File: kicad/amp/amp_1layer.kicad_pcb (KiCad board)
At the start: 2 copper layers, 194.3 x 100 mm, 134 parts, among them J1 DC 12V IN, J2 IN L-G-R, J3 SPK L, J4 SPK R, Q1001 BC547, Q1002 BC547, Q1003 BC557, Q1004 BD139, Q1005 BD140, Q1006 BC547, Q2001 BC547, Q2002 BC547, Q2003 BC557, Q2004 BD139, Q2005 BD140, Q2006 BC547

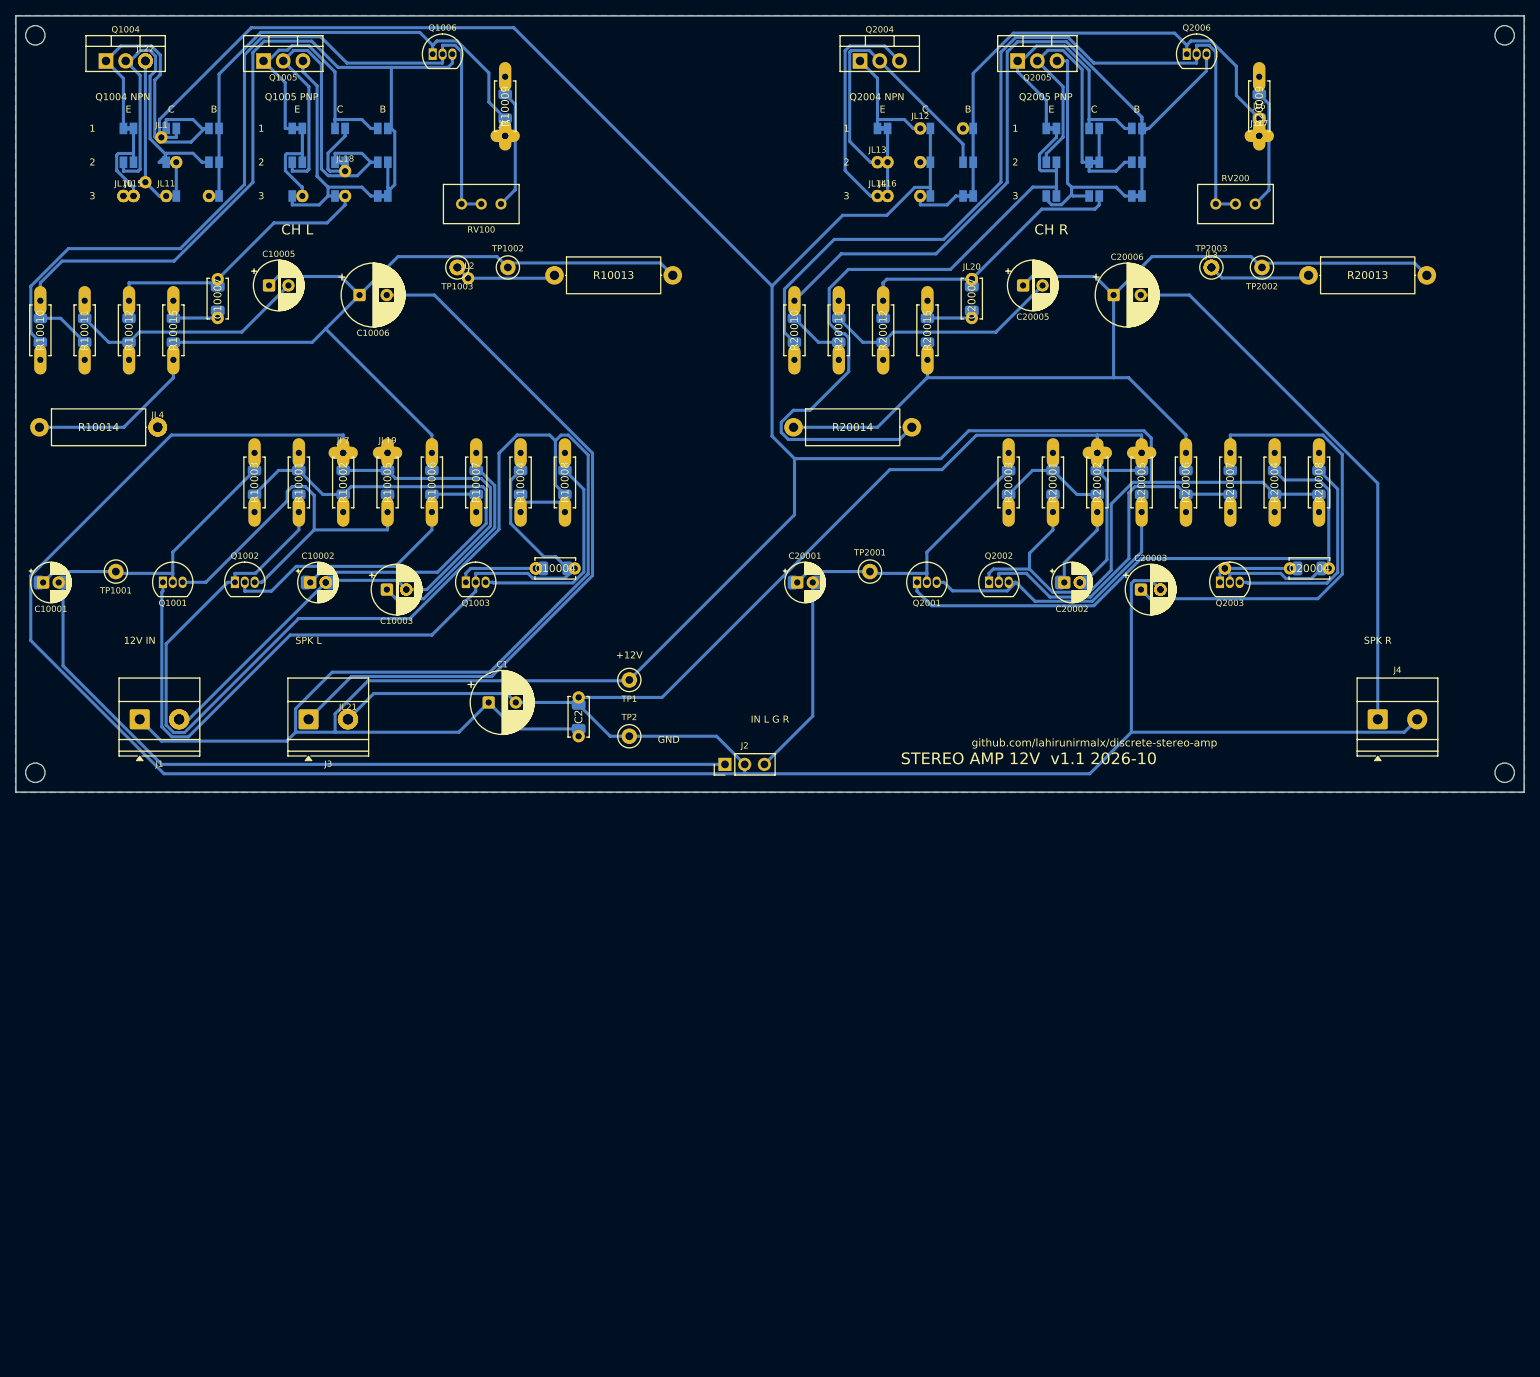
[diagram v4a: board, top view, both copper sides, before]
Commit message: Release 1.2: mirror-loaded front end, closed-loop PSU, VU tap, headphone board
- Amp: PNP input pair with NPN current-mirror load, LED-referenced current-source tail,
  NPN VAS with bootstrapped load from +12V, 220p Miller + 47p lead cap (THD 0.004% at 26 mW/8R,
  0.019% at 0.29 W; was 0.03 / 0.2). 1k VU meter tap per channel to header J5.
- PSU: BC547 error amplifier, 5.6 V zener fed from VOUT, 8.2k + 2k trimmer / 10k divider,
  2.2k drive, 47n/100n compensation. 12.0 V set point, 0.14 V dip on a 1 A step.
- New headphone board (DPDT switch, 120R series, DIRECT jumpers, 3.5 mm jack, panel-jack header).
- Boards: amp 134x85 / compact 100x98, PSU 90x58, hp 42x30; panel 155x155 with four boards.
  All 2-layer boards and the panel DRC clean; single-sided amp down to 15 errors.
- Toolchain: STAMP constant, reroute.sh second routing pass, rotated titles, link holes on
  jumper pads, 2 mm routing corridor per channel.
- Docs, BOMs, order guide, changelog, known issues rewritten for release 2.
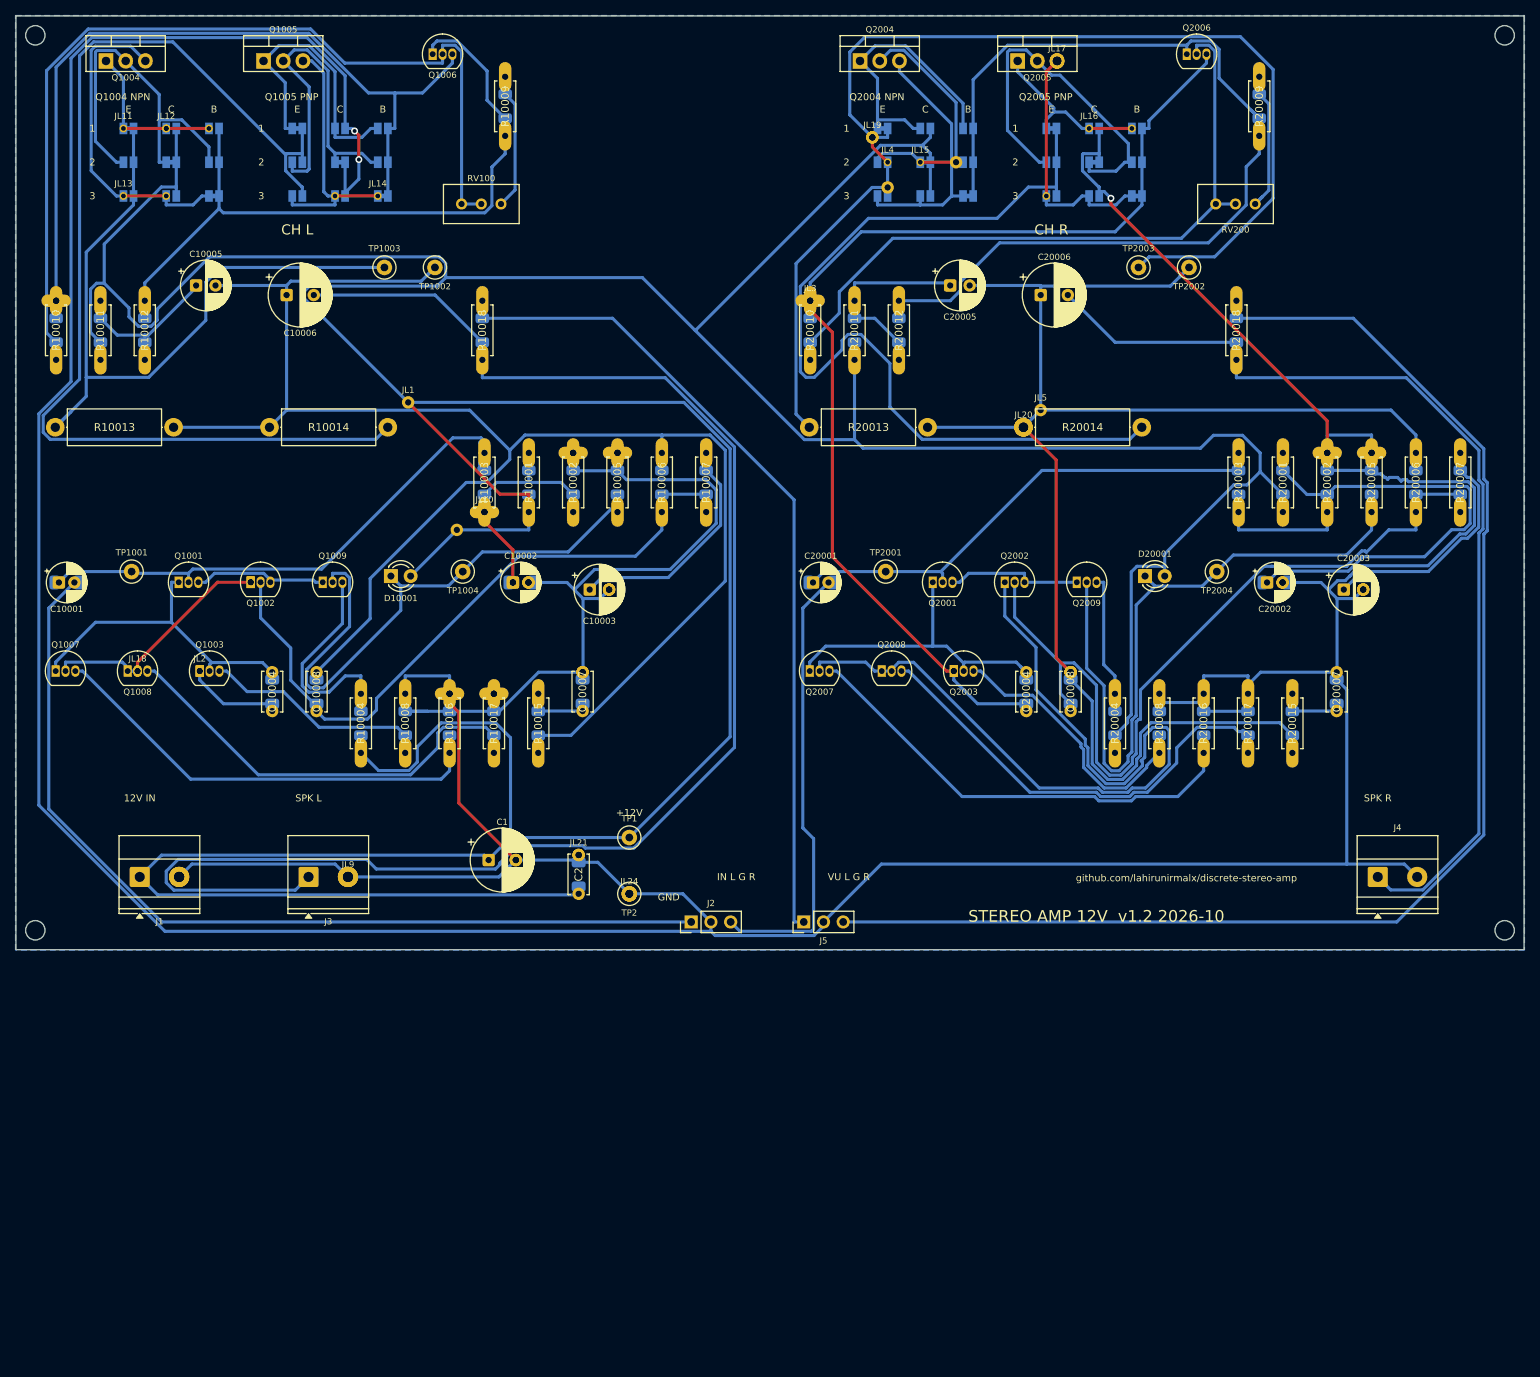
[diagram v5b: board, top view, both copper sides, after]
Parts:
- added C10008: 47p, Custom:C_P5_1206, F.Cu at (88.7, 139.6)
- added C20008: 47p, Custom:C_P5_1206, F.Cu at (185.9, 139.6)
- added D10001: LED red, LED_THT:LED_D3.0mm, F.Cu at (98.3, 122.2)
- added D20001: LED red, LED_THT:LED_D3.0mm, F.Cu at (195.5, 122.2)
- added J5: VU L-G-R, Connector_PinHeader_2.54mm:PinHeader_1x03_P2.54mm_Vertical, F.Cu at (151.5, 166.7)
- added JL23: wire link, Custom:WireLink, F.Cu at (116.0, 123.0)
- added JL24: wire link, Custom:WireLink, F.Cu at (129.0, 163.1)
- added Q1007: BC547, Custom:TO92_SOT23, F.Cu at (55.1, 134.4)
- added Q1008: BC547, Custom:TO92_SOT23, F.Cu at (64.4, 134.4)
- added Q1009: BC557, Custom:TO92_SOT23, F.Cu at (89.5, 123.0)
- added Q2007: BC547, Custom:TO92_SOT23, F.Cu at (152.3, 134.4)
- added Q2008: BC547, Custom:TO92_SOT23, F.Cu at (161.5, 134.4)
- added Q2009: BC557, Custom:TO92_SOT23, F.Cu at (186.7, 123.0)
- added R10016: 100, Custom:R_Axial_1206, F.Cu at (105.9, 144.9)
- added R10017: 100, Custom:R_Axial_1206, F.Cu at (111.6, 144.9)
- added R10018: 1k, Custom:R_Axial_1206, F.Cu at (110.1, 94.3)
- added R20016: 100, Custom:R_Axial_1206, F.Cu at (203.0, 144.9)
- added R20017: 100, Custom:R_Axial_1206, F.Cu at (208.7, 144.9)
- added R20018: 1k, Custom:R_Axial_1206, F.Cu at (207.2, 94.3)
- added TP1004: LED 10.2V, TestPoint:TestPoint_Loop_D2.50mm_Drill1.0mm, F.Cu at (107.6, 121.6)
- added TP2004: LED 10.2V, TestPoint:TestPoint_Loop_D2.50mm_Drill1.0mm, F.Cu at (204.7, 121.6)
- C10004, C20004: value 100p -> 220p
- Q1001, Q1002, Q2001, Q2002: value BC547 -> BC557
- Q1003, Q2003: value BC557 -> BC547
- R10004, R20004: value 4.7k -> 1.2k
- R10005, R20005: value 10k -> 4.7k
- TP1001, TP2001: value B1 5.9V -> B1 6.1V
- moved JL22 161.2 mm to (213.2, 123.0)
- moved JL6 135.3 mm to (114.4, 158.8)
- moved JL7 132.6 mm to (223.6, 123.9)
- moved JL9 111.0 mm to (92.8, 160.9)
- moved JL15 101.5 mm to (166.5, 68.8)
- moved JL4 100.0 mm to (162.3, 68.8)
- moved JL13 97.2 mm to (63.9, 73.2)
- moved JL12 97.1 mm to (69.4, 64.5)
- moved JL5 77.5 mm to (182.0, 100.8)
- moved JL19 74.5 mm to (160.3, 65.7)
- moved JL8 71.0 mm to (126.4, 123.9)
- moved JL18 69.7 mm to (65.7, 134.4)
- moved R10015 69.1 mm to (117.3, 144.9)
- moved R20015 69.1 mm to (214.4, 144.9)
- moved C10007 69.1 mm to (123.0, 139.6)
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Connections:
- C10004 pad 1: /VAS_L -> /B5_L
- C10004 pad 1S: /VAS_L -> /B5_L
- C10005 pad 1: /OUT_L -> Net-(C10005-Pad1)
- C10005 pad 2: Net-(C10005-Pad2) -> /OUT_L
- C20004 pad 1: /VAS_R -> /B5_R
- C20004 pad 1S: /VAS_R -> /B5_R
- C20005 pad 1: /OUT_R -> Net-(C20005-Pad1)
- C20005 pad 2: Net-(C20005-Pad2) -> /OUT_R
- JL10 pad 1: Net-(JP10007-A) -> Net-(C10002-Pad1)
- JL10 pad 2: Net-(JP10007-A) -> Net-(C10002-Pad1)
- JL11 pad 1: Net-(JP10007-A) -> Net-(JP10001-A)
- JL11 pad 2: Net-(JP10007-A) -> Net-(JP10001-A)
- JL12 pad 1: Net-(JP20001-A) -> Net-(JP10001-A)
- JL12 pad 2: Net-(JP20001-A) -> Net-(JP10001-A)
- JL13 pad 1: Net-(JP20004-A) -> Net-(JP10007-A)
- JL13 pad 2: Net-(JP20004-A) -> Net-(JP10007-A)
- JL14 pad 1: Net-(JP20007-A) -> Net-(JP10017-A)
- JL14 pad 2: Net-(JP20007-A) -> Net-(JP10017-A)
- JL15 pad 1: /E4_L -> Net-(JP20004-A)
- JL15 pad 2: /E4_L -> Net-(JP20004-A)
- JL16 pad 1: /E4_R -> Net-(JP20014-A)
- JL16 pad 2: /E4_R -> Net-(JP20014-A)
- JL17 pad 1: /VAS_R -> Net-(JP20017-A)
- JL17 pad 2: /VAS_R -> Net-(JP20017-A)
- JL18 pad 1: GND -> Net-(Q1002-C)
- JL18 pad 2: GND -> Net-(Q1002-C)
- JL19 pad 1: GND -> /E4_R
- JL19 pad 2: GND -> /E4_R
- JL2 pad 1: /E4_L -> /B5_L
- JL2 pad 2: /E4_L -> /B5_L
- JL20 pad 1: GND -> /OUT_R
- JL20 pad 2: GND -> /OUT_R
- JL22 pad 1: Net-(JP10007-A) -> GND
- JL22 pad 2: Net-(JP10007-A) -> GND
- JL3 pad 1: /E4_R -> /B5_R
- JL3 pad 2: /E4_R -> /B5_R
- JL4 pad 1: /E5_L -> /E4_R
- JL4 pad 2: /E5_L -> /E4_R
- JL5 pad 1: /VAS_L -> /OUT_R
- JL5 pad 2: /VAS_L -> /OUT_R
- JL6 pad 1: /VAS_R -> GND
- JL6 pad 2: /VAS_R -> GND
- Q1002 pad 1: +12V -> Net-(Q1002-C)
- Q1003 pad 1: /VAS_L -> /B5_L
- Q2002 pad 1: +12V -> Net-(Q2002-C)
- Q2003 pad 1: /VAS_R -> /B5_R
- R10004 pad 2: Net-(Q1001-C) -> Net-(Q1009-E)
- R10004 pad 2S: Net-(Q1001-C) -> Net-(Q1009-E)
- R10005 pad 1: Net-(Q1001-E) -> Net-(D10001-K)
- R10005 pad 1S: Net-(Q1001-E) -> Net-(D10001-K)
- R10008 pad 1: +12V -> Net-(Q1003-E)
- R10008 pad 1S: +12V -> Net-(Q1003-E)
- R10008 pad 2: Net-(Q1003-E) -> GND
- R10008 pad 2S: Net-(Q1003-E) -> GND
- R10011 pad 1: /B5_L -> +12V
- R10011 pad 1S: /B5_L -> +12V
- R10011 pad 2: Net-(C10005-Pad2) -> Net-(C10005-Pad1)
- R10011 pad 2S: Net-(C10005-Pad2) -> Net-(C10005-Pad1)
- R10012 pad 1: Net-(C10005-Pad2) -> Net-(C10005-Pad1)
- R10012 pad 1S: Net-(C10005-Pad2) -> Net-(C10005-Pad1)
- R10012 pad 2: GND -> /VAS_L
- R10012 pad 2S: GND -> /VAS_L
- R20004 pad 2: Net-(Q2001-C) -> Net-(Q2009-E)
- R20004 pad 2S: Net-(Q2001-C) -> Net-(Q2009-E)
- R20005 pad 1: Net-(Q2001-E) -> Net-(D20001-K)
- R20005 pad 1S: Net-(Q2001-E) -> Net-(D20001-K)
- R20008 pad 1: +12V -> Net-(Q2003-E)
- R20008 pad 1S: +12V -> Net-(Q2003-E)
- R20008 pad 2: Net-(Q2003-E) -> GND
- R20008 pad 2S: Net-(Q2003-E) -> GND
- R20011 pad 1: /B5_R -> +12V
- R20011 pad 1S: /B5_R -> +12V
- R20011 pad 2: Net-(C20005-Pad2) -> Net-(C20005-Pad1)
- R20011 pad 2S: Net-(C20005-Pad2) -> Net-(C20005-Pad1)
- R20012 pad 1: Net-(C20005-Pad2) -> Net-(C20005-Pad1)
- R20012 pad 1S: Net-(C20005-Pad2) -> Net-(C20005-Pad1)
- R20012 pad 2: GND -> /VAS_R
- R20012 pad 2S: GND -> /VAS_R
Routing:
- net /VU_R: track 0.00 -> 178.4 mm
- net GND: track 616.7 -> 776.0 mm, vias 0 -> 3
- net /E4_R: track 21.9 -> 157.3 mm
- net /E5_L: track 12.8 -> 142.0 mm
- net /SPK_L: track 95.0 -> 205.8 mm
- net /VU_L: track 0.00 -> 107.7 mm
- net Net-(Q2002-C): track 0.00 -> 105.0 mm
- net Net-(D20001-K): track 0.00 -> 94.1 mm
- net /OUT_L: track 131.9 -> 219.7 mm
- net Net-(D10001-K): track 0.00 -> 77.8 mm
- net /OUT_R: track 133.0 -> 203.1 mm
- net /E4_L: track 26.0 -> 92.6 mm
- net Net-(Q2002-B): track 48.1 -> 112.8 mm
- net Net-(Q1001-C): track 103.5 -> 42.1 mm
- net Net-(Q2007-E): track 0.00 -> 61.3 mm
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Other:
- board size 194.3 x 100 mm -> 194.3 x 120.3 mm
- board text added: "STEREO AMP 12V v1.2 2026-10"
- board text added: "VU L G R"
- board text removed: "STEREO AMP 12V v1.1 2026-10"
